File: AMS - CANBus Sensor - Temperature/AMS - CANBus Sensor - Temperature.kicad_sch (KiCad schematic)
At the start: 16 parts, among them J1 Power_And_CAN, J2 Power_And_CAN, J6 Screw_Terminal_01x02, Q1 IRF9Z34NPBF, U1 3568, U5 3568

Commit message: wip for the temp sensor
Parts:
- removed J2: Power_And_CAN, TerminalBlock_Phoenix:TerminalBlock_Phoenix_MPT-0,5-4-2.54_1x04_P2.54mm_Horizontal, symbol Connector:Screw_Terminal_01x04
- removed J6: Screw_Terminal_01x02, TerminalBlock_Phoenix:TerminalBlock_Phoenix_MPT-0,5-2-2.54_1x02_P2.54mm_Horizontal, symbol Connector:Screw_Terminal_01x02
- removed RV1, RV2, RV3, RV4: 200k, Potentiometer_THT:Potentiometer_Bourns_3296W_Vertical, symbol Device:R_Potentiometer_US
- removed U1: 3568, 3568, symbol SamacSys_Parts:3568
- added C17: 22uf, Capacitor_SMD:C_1206_3216Metric_Pad1.33x1.80mm_HandSolder, symbol Device:C
- added IC4: CD74HC4050ME4, SOIC127P600X175-16N, symbol SamacSys_Parts:CD74HC4050ME4
- added IC5: AZ1117CH2-3.3TRG1, SOT230P700X180-4N, symbol SamacSys_Parts:AZ1117CH2-3.3TRG1
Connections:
- net +5V: now also IC5.1 (INPUT)
- net BareMinAtmel328P/PD3-D3: now also IC4.14 (6A)
- net BareMinAtmel328P/PD4-D4: now also IC4.11 (5A)
- net BareMinAtmel328P/PD5-D5: now also IC4.9 (4A)
- net GND: now also C17.1, IC4.8 (GND), IC5.2 (ADJ/GND_1), IC5.4 (ADJ/GND_2)
- new net +3.3V: C17.2, IC4.1 (VCC), IC5.3 (OUTPUT)
- new net CLK: IC4.3 (1A)
- new net MAX31865AAP+1/CS3v: IC4.15 (6Y)
- new net MAX31865AAP+1/MISO3v: IC4.5 (2A)
- new net MAX31865AAP+1/MOSI3v: IC4.6 (3Y)
- new net MAX31865AAP+1/SLC3v: IC4.2 (1Y)
- new net MAX31865AAP+2/CS3v: IC4.12 (5Y)
- new net MAX31865AAP+3/CS3v: IC4.10 (4Y)
- new net MISO: IC4.4 (2Y)
- new net MOSI: IC4.7 (3A)
- no-connect marks 12 -> 15
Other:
- removed sheet BufferedADC
- added sheet MAX31865AAP+1 (MAX31865AAP+.kicad_sch)
- added sheet MAX31865AAP+2 (MAX31865AAP+.kicad_sch)
- added sheet MAX31865AAP+3 (MAX31865AAP+.kicad_sch)
- moved on the sheet: NTC1, R2, R3, Reset1

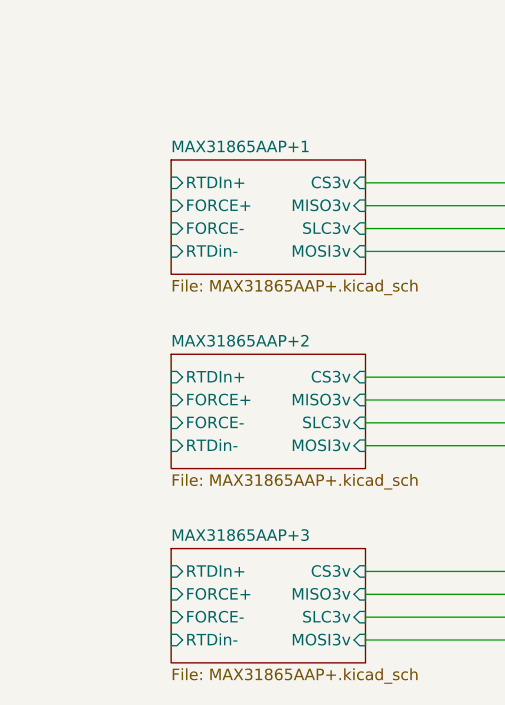
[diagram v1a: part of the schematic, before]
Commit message: Temp Sensor Done
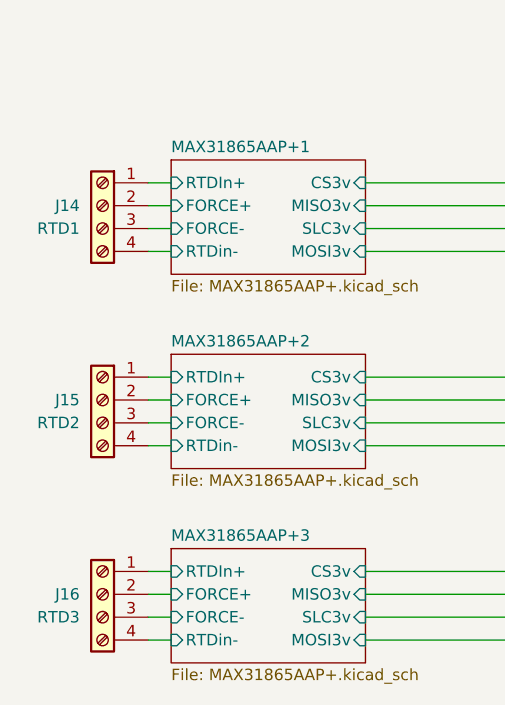
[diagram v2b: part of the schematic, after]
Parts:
- added J14: RTD1, TerminalBlock_Phoenix:TerminalBlock_Phoenix_MPT-0,5-4-2.54_1x04_P2.54mm_Horizontal, symbol Connector:Screw_Terminal_01x04
- added J15: RTD2, TerminalBlock_Phoenix:TerminalBlock_Phoenix_MPT-0,5-4-2.54_1x04_P2.54mm_Horizontal, symbol Connector:Screw_Terminal_01x04
- added J16: RTD3, TerminalBlock_Phoenix:TerminalBlock_Phoenix_MPT-0,5-4-2.54_1x04_P2.54mm_Horizontal, symbol Connector:Screw_Terminal_01x04
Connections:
- net MAX31865AAP+1/FORCE+: now also J14.2 (Pin_2)
- net MAX31865AAP+1/FORCE-: now also J14.3 (Pin_3)
- net MAX31865AAP+1/RTDIn+: now also J14.1 (Pin_1)
- net MAX31865AAP+1/RTDin-: now also J14.4 (Pin_4)
- net MAX31865AAP+2/FORCE+: now also J15.2 (Pin_2)
- net MAX31865AAP+2/FORCE-: now also J15.3 (Pin_3)
- net MAX31865AAP+2/RTDIn+: now also J15.1 (Pin_1)
- net MAX31865AAP+2/RTDin-: now also J15.4 (Pin_4)
- net MAX31865AAP+3/FORCE+: now also J16.2 (Pin_2)
- net MAX31865AAP+3/FORCE-: now also J16.3 (Pin_3)
- net MAX31865AAP+3/RTDIn+: now also J16.1 (Pin_1)
- net MAX31865AAP+3/RTDin-: now also J16.4 (Pin_4)

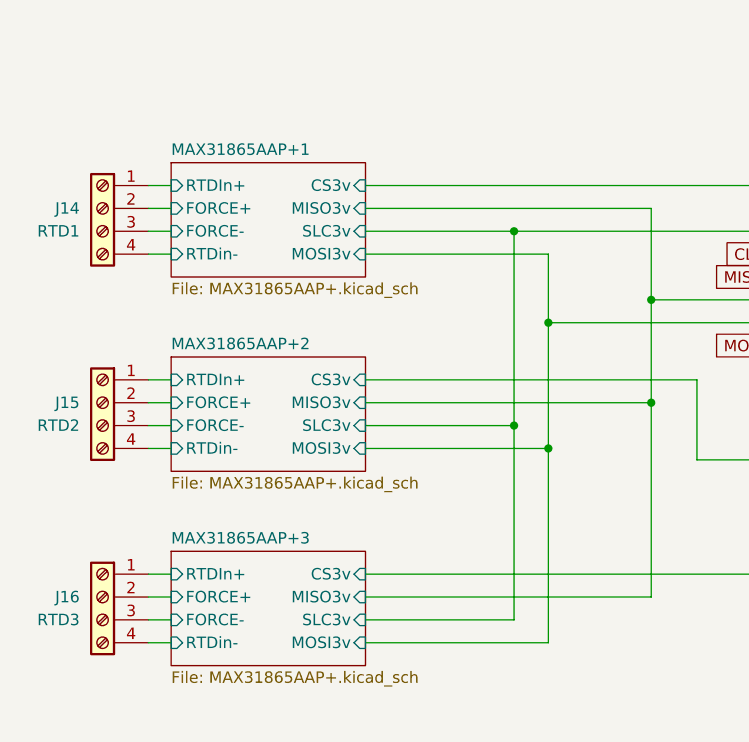
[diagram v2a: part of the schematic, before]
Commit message: update for my screw up for the power to the RTD chips
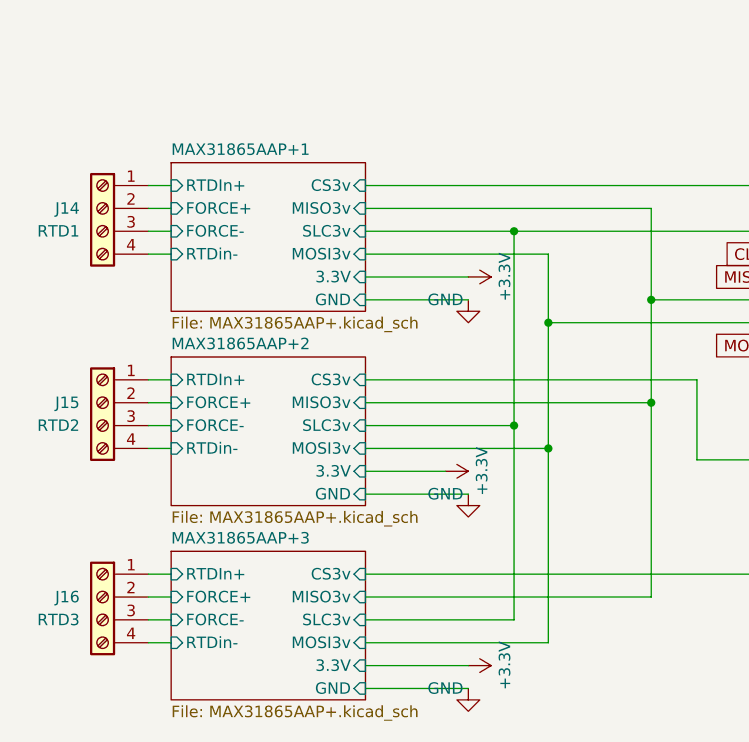
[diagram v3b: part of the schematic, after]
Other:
- sheet MAX31865AAP+1 ports: added 3.3V, GND; removed none
- sheet MAX31865AAP+2 ports: added 3.3V, GND; removed none
- sheet MAX31865AAP+3 ports: added 3.3V, GND; removed none
